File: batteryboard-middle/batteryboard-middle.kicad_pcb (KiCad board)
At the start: 2 copper layers, 46.8 x 46.8 mm, 9 parts, among them J1 Conn_02x05_Odd_Even, J2 Conn_01x02, J3 Conn_01x02, J4 Conn_02x05_Odd_Even

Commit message: Recheck boards and re-export models
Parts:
- J1: value Conn_02x05_Odd_Even -> FLE-105-01-G-DV-A
- J4: value Conn_02x05_Odd_Even -> FTS-105-01-L-DV-A
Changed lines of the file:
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@@
       (effects (font (size 1.27 1.27) (thickness 0.254)))
     )
-    (fp_text value "Conn_02x05_Odd_Even" (at 0 0 90) (layer "F.SilkS") hide
+    (fp_text value "FTS-105-01-L-DV-A" (at 0 0 90) (layer "F.SilkS") hide
       (effects (font (size 1.27 1.27) (thickness 0.254)))
     )
@@
       (effects (font (size 1 1) (thickness 0.15)) (justify mirror))
     )
-    (fp_text value "Conn_02x05_Odd_Even" (at 11.065 -4.31 90) (layer "B.Fab")
+    (fp_text value "FLE-105-01-G-DV-A" (at 11.065 -4.31 90) (layer "B.Fab")
       (effects (font (size 1 1) (thickness 0.15)) (justify mirror))
     )
+    (fp_line (start 3.26 -1.665) (end 3.26 1.665) (layer "B.SilkS") (width 0.2))
     (fp_line (start -3.26 -1.665) (end -3.26 1.665) (layer "B.SilkS") (width 0.2))
-    (fp_line (start 3.26 -1.665) (end 3.26 1.665) (layer "B.SilkS") (width 0.2))
     (fp_circle (center -2.85 3.44) (end -2.75 3.44) (layer "B.SilkS") (width 0.2) (fill none))
+    (fp_line (start 3.425 2.93) (end 3.425 -2.93) (layer "B.CrtYd") (width 0.05))
+    (fp_line (start 3.425 -2.93) (end -3.425 -2.93) (layer "B.CrtYd") (width 0.05))
+    (fp_line (start -3.425 2.93) (end 3.425 2.93) (layer "B.CrtYd") (width 0.05))
     (fp_line (start -3.425 -2.93) (end -3.425 2.93) (layer "B.CrtYd") (width 0.05))
-    (fp_line (start -3.425 2.93) (end 3.425 2.93) (layer "B.CrtYd") (width 0.05))
-    (fp_line (start 3.425 -2.93) (end -3.425 -2.93) (layer "B.CrtYd") (width 0.05))
-    (fp_line (start 3.425 2.93) (end 3.425 -2.93) (layer "B.CrtYd") (width 0.05))
     (fp_line (start 3.175 1.665) (end 3.175 -1.665) (layer "B.Fab") (width 0.1))
     (fp_line (start -3.175 1.665) (end 3.175 1.665) (layer "B.Fab") (width 0.1))
@@
     (fp_line (start -3.175 -1.665) (end -3.175 1.665) (layer "B.Fab") (width 0.1))
     (fp_circle (center -2.85 3.44) (end -2.75 3.44) (layer "B.Fab") (width 0.2) (fill none))
+    (pad "" np_thru_hole circle (at 1.905 0 90) (size 0.76 0.76) (drill 0.76) (layers *.Cu *.Mask))
     (pad "" np_thru_hole circle (at -1.905 0 90) (size 0.76 0.76) (drill 0.76) (layers *.Cu *.Mask))
-    (pad "" np_thru_hole circle (at 1.905 0 90) (size 0.76 0.76) (drill 0.76) (layers *.Cu *.Mask))
-    (pad "01" smd rect (at -2.54 1.8425 90) (size 0.74 1.675) (layers "B.Cu" "B.Paste" "B.Mask")
+    (pad "1" smd rect (at -2.54 1.8425 90) (size 0.74 1.675) (layers "B.Cu" "B.Paste" "B.Mask")
       (net 1 "BATT_P_SW") (pinfunction "Pin_1") (pintype "passive"))
-    (pad "02" smd rect (at -2.54 -1.8425 90) (size 0.74 1.675) (layers "B.Cu" "B.Paste" "B.Mask")
+    (pad "2" smd rect (at -2.54 -1.8425 90) (size 0.74 1.675) (layers "B.Cu" "B.Paste" "B.Mask")
       (net 2 "BATT_N_SW") (pinfunction "Pin_2") (pintype "passive"))
-    (pad "03" smd rect (at -1.27 1.8425 90) (size 0.74 1.675) (layers "B.Cu" "B.Paste" "B.Mask")
+    (pad "3" smd rect (at -1.27 1.8425 90) (size 0.74 1.675) (layers "B.Cu" "B.Paste" "B.Mask")
       (net 4 "+3V3") (pinfunction "Pin_3") (pintype "passive"))
-    (pad "04" smd rect (at -1.27 -1.8425 90) (size 0.74 1.675) (layers "B.Cu" "B.Paste" "B.Mask")
+    (pad "4" smd rect (at -1.27 -1.8425 90) (size 0.74 1.675) (layers "B.Cu" "B.Paste" "B.Mask")
       (net 3 "GND") (pinfunction "Pin_4") (pintype "passive"))
-    (pad "05" smd rect (at 0 1.8425 90) (size 0.74 1.675) (layers "B.Cu" "B.Paste" "B.Mask")
+    (pad "5" smd rect (at 0 1.8425 90) (size 0.74 1.675) (layers "B.Cu" "B.Paste" "B.Mask")
       (net 5 "SDA3") (pinfunction "Pin_5") (pintype "passive"))
-    (pad "06" smd rect (at 0 -1.8425 90) (size 0.74 1.675) (layers "B.Cu" "B.Paste" "B.Mask")
+    (pad "6" smd rect (at 0 -1.8425 90) (size 0.74 1.675) (layers "B.Cu" "B.Paste" "B.Mask")
       (net 6 "SCL3") (pinfunction "Pin_6") (pintype "passive"))
-    (pad "07" smd rect (at 1.27 1.8425 90) (size 0.74 1.675) (layers "B.Cu" "B.Paste" "B.Mask")
+    (pad "7" smd rect (at 1.27 1.8425 90) (size 0.74 1.675) (layers "B.Cu" "B.Paste" "B.Mask")
       (net 7 "COIL_P") (pinfunction "Pin_7") (pintype "passive"))
-    (pad "08" smd rect (at 1.27 -1.8425 90) (size 0.74 1.675) (layers "B.Cu" "B.Paste" "B.Mask")
+    (pad "8" smd rect (at 1.27 -1.8425 90) (size 0.74 1.675) (layers "B.Cu" "B.Paste" "B.Mask")
       (net 8 "COIL_N") (pinfunction "Pin_8") (pintype "passive"))
-    (pad "09" smd rect (at 2.54 1.8425 90) (size 0.74 1.675) (layers "B.Cu" "B.Paste" "B.Mask")
+    (pad "9" smd rect (at 2.54 1.8425 90) (size 0.74 1.675) (layers "B.Cu" "B.Paste" "B.Mask")
       (net 9 "BATT_P") (pinfunction "Pin_9") (pintype "passive"))
     (pad "10" smd rect (at 2.54 -1.8425 90) (size 0.74 1.675) (layers "B.Cu" "B.Paste" "B.Mask")
       (net 10 "VBUS") (pinfunction "Pin_10") (pintype "passive"))
-    (model "C:/Users/Neil/Desktop/avionics-batteryboard/kicad-libs/3d/FLE-105-01-G-DV-A.step" hide
+    (model "${KIPRJMOD}/../kicad-libs/3d/FLE-105-01-G-DV-A.step"
       (offset (xyz 0 0 0.1524))
       (scale (xyz 1 1 1))
@@
   (segment (start 132.2 97.787612) (end 125.935512 91.523124) (width 0.635) (layer "B.Cu") (net 2))
   (segment (start 132.2 110.129189) (end 132.2 97.787612) (width 0.635) (layer "B.Cu") (net 2))
-  (via (at 125.9 90.2) (size 0.8) (drill 0.4) (layers "F.Cu" "B.Cu") (net 3))
-  (via (at 129.7 90.2) (size 0.8) (drill 0.4) (layers "F.Cu" "B.Cu") (net 4))
-  (via (at 129.7 89) (size 0.8) (drill 0.4) (layers "F.Cu" "B.Cu") (net 5))
-  (via (at 125.9 89) (size 0.8) (drill 0.4) (layers "F.Cu" "B.Cu") (net 6))
-  (via (at 129.7 87.7) (size 0.8) (drill 0.4) (layers "F.Cu" "B.Cu") (net 7))
-  (via (at 125.9 87.7) (size 0.8) (drill 0.4) (layers "F.Cu" "B.Cu") (net 8))
-  (via (at 129.7 86.4) (size 0.8) (drill 0.4) (layers "F.Cu" "B.Cu") (net 9))
-  (via (at 125.9 86.4) (size 0.8) (drill 0.4) (layers "F.Cu" "B.Cu") (net 10))
+  (via (at 125.9 90.25) (size 0.8) (drill 0.4) (layers "F.Cu" "B.Cu") (net 3))
+  (via (at 129.7 90.25) (size 0.8) (drill 0.4) (layers "F.Cu" "B.Cu") (net 4))
+  (via (at 129.7 88.975) (size 0.8) (drill 0.4) (layers "F.Cu" "B.Cu") (net 5))
+  (via (at 125.9 88.975) (size 0.8) (drill 0.4) (layers "F.Cu" "B.Cu") (net 6))
+  (via (at 129.7 87.725) (size 0.8) (drill 0.4) (layers "F.Cu" "B.Cu") (net 7))
+  (via (at 125.9 87.725) (size 0.8) (drill 0.4) (layers "F.Cu" "B.Cu") (net 8))
+  (via (at 129.7 86.45) (size 0.8) (drill 0.4) (layers "F.Cu" "B.Cu") (net 9))
+  (via (at 125.9 86.45) (size 0.8) (drill 0.4) (layers "F.Cu" "B.Cu") (net 10))
   (zone (net 3) (net_name "GND") (layers F&B.Cu) (hatch edge 0.508)
     (connect_pads yes (clearance 0.381))

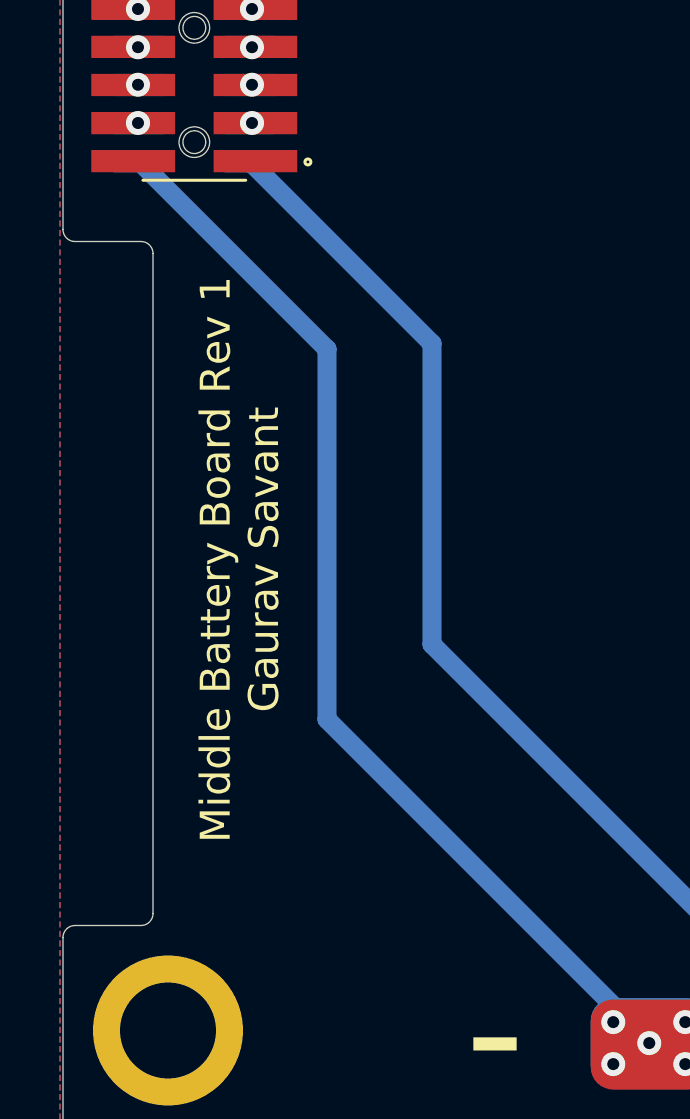
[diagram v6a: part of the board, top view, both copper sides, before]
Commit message: modified/standardized silkscreen
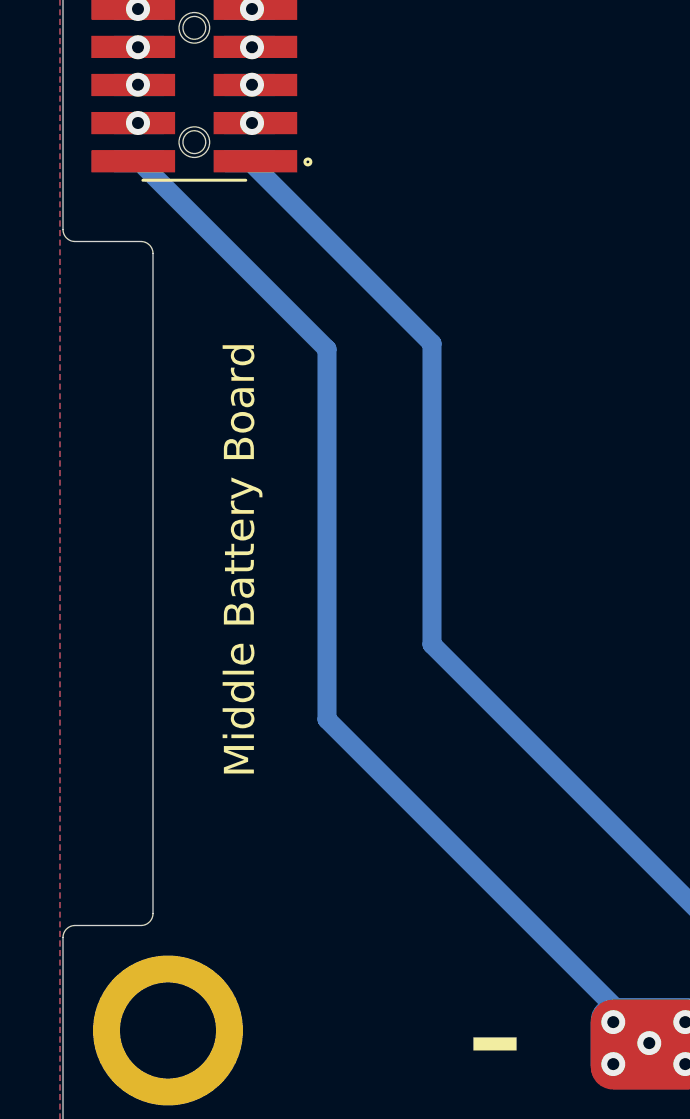
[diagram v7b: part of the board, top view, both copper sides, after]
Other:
- board text added: "Middle Battery Board"
- board text removed: "Middle Battery Board Rev 1 Gaurav Savant"
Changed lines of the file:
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@@
     (effects (font (size 4 4) (thickness 0.7)) (justify mirror))
   )
-  (gr_text "Middle Battery Board Rev 1\nGaurav Savant\n" (at 129.3 104.8 90) (layer "F.SilkS")
+  (gr_text "Middle Battery Board\n" (at 129.3 104.8 90) (layer "F.SilkS")
     (effects (font (size 1 1) (thickness 0.15)))
   )

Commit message: Export New Gerbers
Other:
- board text added: "06-JUL-22"
- board text added: "v01.1"
- board text removed: "09-JUN-22"
- board text removed: "v01"
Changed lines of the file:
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@@
       (outputformat 1)
       (mirror false)
-      (drillshape 1)
+      (drillshape 0)
       (scaleselection 1)
-      (outputdirectory "")
+      (outputdirectory "../gerbers/batteryboard-middle (07-06-22)/")
     )
   )
@@
     (effects (font (size 4 4) (thickness 0.7)) (justify mirror))
   )
-  (gr_text "Middle Battery Board\n" (at 129.3 104.8 90) (layer "F.SilkS")
-    (effects (font (size 1 1) (thickness 0.15)))
+  (gr_text "Middle Battery Board\n" (at 128.175 105.775 90) (layer "F.SilkS")
+    (effects (font (size 0.889 0.889) (thickness 0.127)))
   )
   (gr_text "-" (at 137.8 120.6) (layer "F.SilkS")
     (effects (font (size 4 4) (thickness 0.7)) (justify mirror))
   )
-  (gr_text "09-JUN-22" (at 148.7 79.9) (layer "F.Mask")
+  (gr_text "06-JUL-22" (at 148.7 79.9) (layer "F.Mask")
     (effects (font (size 0.635 0.635) (thickness 0.1524)) (justify right))
   )
-  (gr_text "v01" (at 150.681203 82.287588) (layer "F.Mask")
+  (gr_text "v01.1" (at 150.681203 82.287588) (layer "F.Mask")
     (effects (font (size 0.635 0.635) (thickness 0.1524)) (justify right))
   )
